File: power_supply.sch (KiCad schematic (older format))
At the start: 20 parts

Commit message: finish scheme & change libs path
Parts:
- gave numbers to parts that had none: 20
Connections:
- net +12V_B renamed FUEL_ADC_POWER
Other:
- note added: "two separate module on 1 PCB\n- module B powered from Vbatt\n- module A powered from IGN\n(Vbatt present always)"

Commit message: specify footpints to resistors and capasitors
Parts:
- C1, C2, C3, C4, C5, C6, C7, C8: footprint (none) -> Capacitors_SMD:C_0805
- U2: footprint TO_SOT_Packages_SMD:TO-263-5_TabPin6 -> zulljon:TO170P1435X457-6N
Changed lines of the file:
@@
 Vbatt
 $Comp
-L GND #PWR05
+L GND #PWR5
 U 1 1 5A05B33F
 P 2400 5550
-F 0 "#PWR05" H 2400 5300 50  0001 C CNN
+F 0 "#PWR5" H 2400 5300 50  0001 C CNN
 F 1 "GND" H 2400 5400 50  0000 C CNN
 F 2 "" H 2400 5550 50  0001 C CNN
@@
 F 0 "C1" H 2475 2250 50  0000 L CNN
 F 1 "100uF" H 2475 2050 50  0000 L CNN
-F 2 "" H 2488 2000 50  0001 C CNN
+F 2 "Capacitors_SMD:C_0805" H 2488 2000 50  0001 C CNN
 F 3 "" H 2450 2150 50  0001 C CNN
 	1    2450 2150
@@
 F 0 "C3" H 5025 2250 50  0000 L CNN
 F 1 "330uF" H 5025 2050 50  0000 L CNN
-F 2 "" H 5038 2000 50  0001 C CNN
+F 2 "Capacitors_SMD:C_0805" H 5038 2000 50  0001 C CNN
 F 3 "" H 5000 2150 50  0001 C CNN
 	1    5000 2150
@@
 	2450 2350 2450 2300
 $Comp
-L GND #PWR06
+L GND #PWR6
 U 1 1 5A05C84D
 P 2550 2400
-F 0 "#PWR06" H 2550 2150 50  0001 C CNN
+F 0 "#PWR6" H 2550 2150 50  0001 C CNN
 F 1 "GND" H 2550 2250 50  0000 C CNN
 F 2 "" H 2550 2400 50  0001 C CNN
@@
 F 0 "C5" H 8325 2200 50  0000 L CNN
 F 1 "100nF" H 8325 2000 50  0000 L CNN
-F 2 "" H 8338 1950 50  0001 C CNN
+F 2 "Capacitors_SMD:C_0805" H 8338 1950 50  0001 C CNN
 F 3 "" H 8300 2100 50  0001 C CNN
 	1    8300 2100
@@
 F 0 "C7" H 9125 2200 50  0000 L CNN
 F 1 "10uF" H 9125 2000 50  0000 L CNN
-F 2 "" H 9138 1950 50  0001 C CNN
+F 2 "Capacitors_SMD:C_0805" H 9138 1950 50  0001 C CNN
 F 3 "" H 9100 2100 50  0001 C CNN
 	1    9100 2100
@@
 	9000 1850 9450 1850
 $Comp
-L GND #PWR07
+L GND #PWR8
 U 1 1 5A05D4B4
 P 8300 2350
-F 0 "#PWR07" H 8300 2100 50  0001 C CNN
+F 0 "#PWR8" H 8300 2100 50  0001 C CNN
 F 1 "GND" H 8300 2200 50  0000 C CNN
 F 2 "" H 8300 2350 50  0001 C CNN
@@
 $EndComp
 $Comp
-L GND #PWR08
+L GND #PWR10
 U 1 1 5A05D4E4
 P 9100 2350
-F 0 "#PWR08" H 9100 2100 50  0001 C CNN
+F 0 "#PWR10" H 9100 2100 50  0001 C CNN
 F 1 "GND" H 9100 2200 50  0000 C CNN
 F 2 "" H 9100 2350 50  0001 C CNN
@@
 F 0 "C6" H 8325 3250 50  0000 L CNN
 F 1 "100nF" H 8325 3050 50  0000 L CNN
-F 2 "" H 8338 3000 50  0001 C CNN
+F 2 "Capacitors_SMD:C_0805" H 8338 3000 50  0001 C CNN
 F 3 "" H 8300 3150 50  0001 C CNN
 	1    8300 3150
@@
 F 0 "C8" H 9125 3250 50  0000 L CNN
 F 1 "10uF" H 9125 3050 50  0000 L CNN
-F 2 "" H 9138 3000 50  0001 C CNN
+F 2 "Capacitors_SMD:C_0805" H 9138 3000 50  0001 C CNN
 F 3 "" H 9100 3150 50  0001 C CNN
 	1    9100 3150
@@
 	9000 2900 9450 2900
 $Comp
-L GND #PWR09
+L GND #PWR9
 U 1 1 5A05D86B
 P 8300 3400
-F 0 "#PWR09" H 8300 3150 50  0001 C CNN
+F 0 "#PWR9" H 8300 3150 50  0001 C CNN
 F 1 "GND" H 8300 3250 50  0000 C CNN
 F 2 "" H 8300 3400 50  0001 C CNN
@@
 $EndComp
 $Comp
-L GND #PWR010
+L GND #PWR11
 U 1 1 5A05D871
 P 9100 3400
-F 0 "#PWR010" H 9100 3150 50  0001 C CNN
+F 0 "#PWR11" H 9100 3150 50  0001 C CNN
 F 1 "GND" H 9100 3250 50  0000 C CNN
 F 2 "" H 9100 3400 50  0001 C CNN
@@
 F 0 "C2" H 2525 3400 50  0000 L CNN
 F 1 "100uF" H 2525 3200 50  0000 L CNN
-F 2 "" H 2538 3150 50  0001 C CNN
+F 2 "Capacitors_SMD:C_0805" H 2538 3150 50  0001 C CNN
 F 3 "" H 2500 3300 50  0001 C CNN
 	1    2500 3300
@@
 F 0 "C4" H 5075 3400 50  0000 L CNN
 F 1 "330uF" H 5075 3200 50  0000 L CNN
-F 2 "" H 5088 3150 50  0001 C CNN
+F 2 "Capacitors_SMD:C_0805" H 5088 3150 50  0001 C CNN
 F 3 "" H 5050 3300 50  0001 C CNN
 	1    5050 3300
@@
 	2500 3500 2500 3450
 $Comp
-L GND #PWR011
+L GND #PWR7
 U 1 1 5A0729CF
 P 2600 3550
-F 0 "#PWR011" H 2600 3300 50  0001 C CNN
+F 0 "#PWR7" H 2600 3300 50  0001 C CNN
 F 1 "GND" H 2600 3400 50  0000 C CNN
 F 2 "" H 2600 3550 50  0001 C CNN
@@
 F 0 "U2" H 3550 3100 50  0000 C CNN
 F 1 "LM2575S-5.0_NOPB" H 3550 2600 50  0000 C CNN
-F 2 "TO_SOT_Packages_SMD:TO-263-5_TabPin6" H 3550 2500 50  0001 C CNN
+F 2 "zulljon:TO170P1435X457-6N" H 3550 2500 50  0001 C CNN
 F 3 "http://www.ti.com/lit/gpn/lm2575" H 3550 2400 50  0001 C CNN
 F 4 "SIMPLE SWITCHER 1.23V to 37V, 1A Low Component Count Step-Down Regulator" H 3550 2300 50  0001 C CNN "Description"

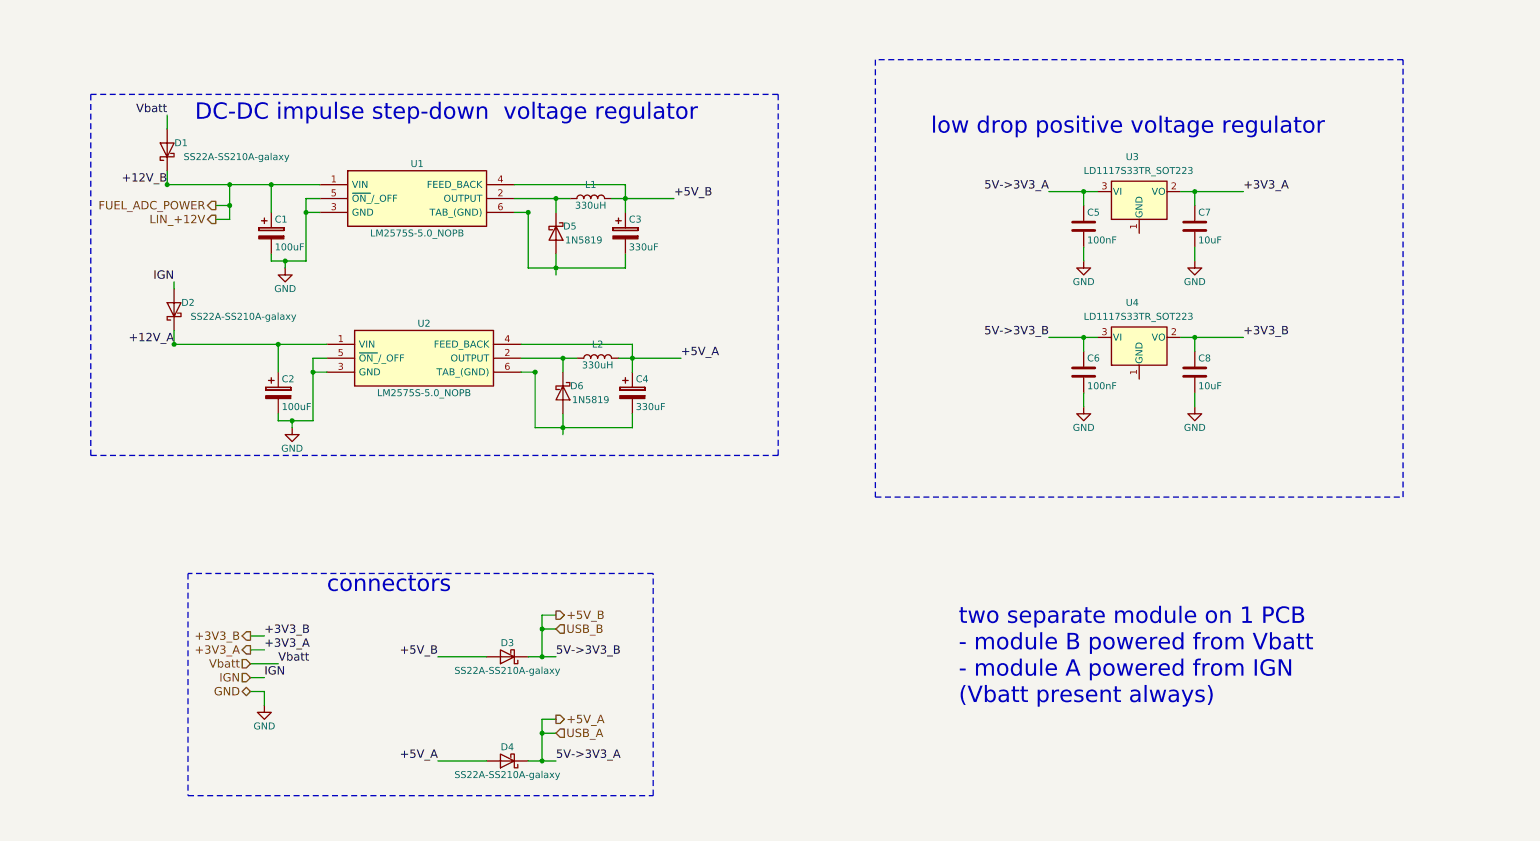
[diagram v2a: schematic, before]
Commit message: add missed footprints, add additional capasitors on 3.3V line, fix banch of ERC errors
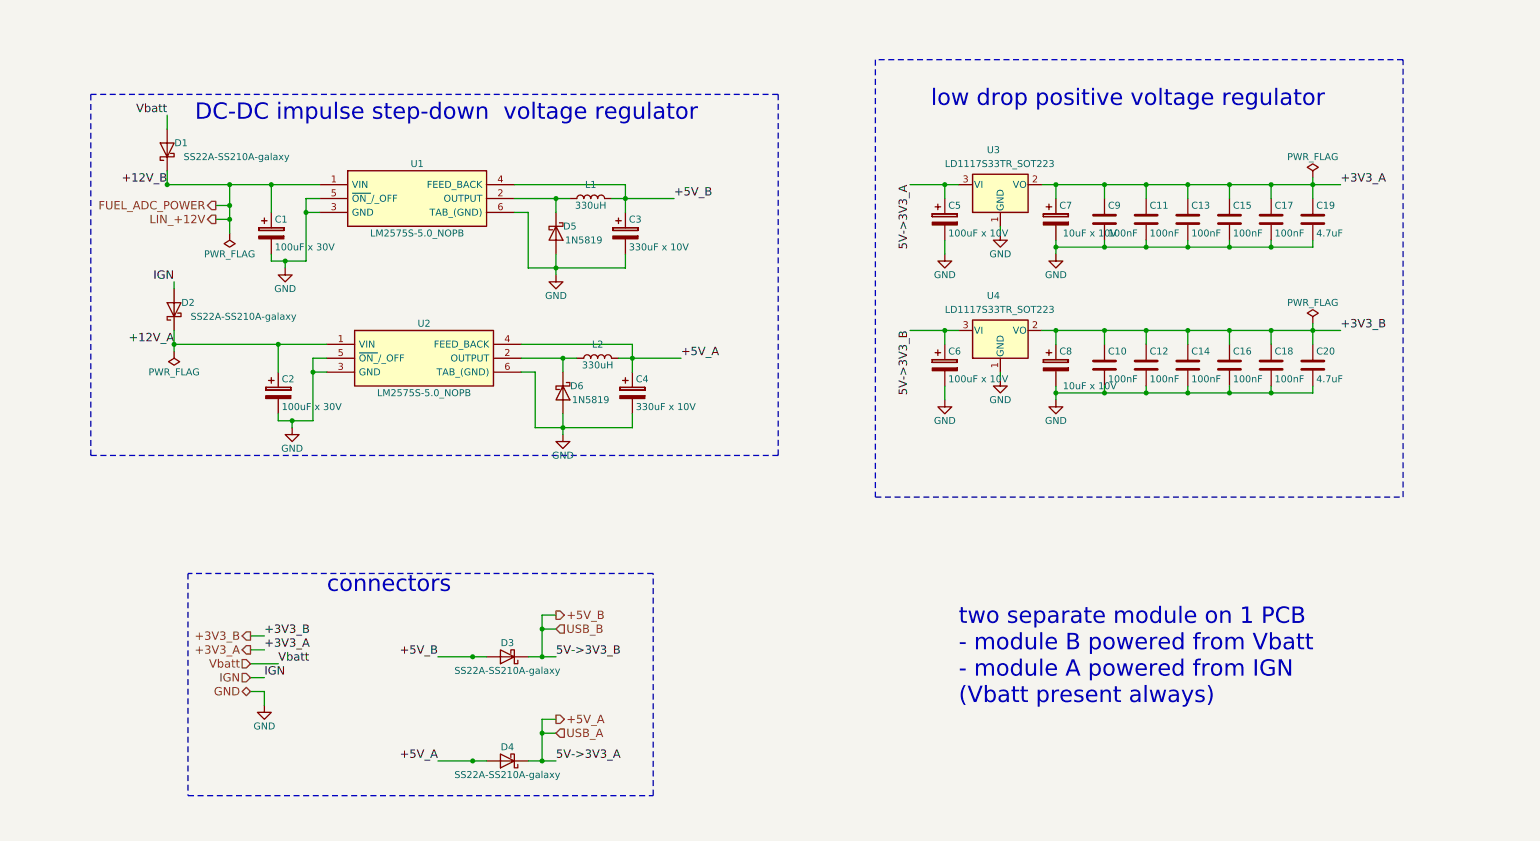
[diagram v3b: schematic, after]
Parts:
- removed C5, C6: 100nF, Capacitors_SMD:C_0805, symbol C
- removed C8: 10uF, Capacitors_SMD:C_0805, symbol C
- added C10, C11, C12, C13, C14, C15, C16, C17, C18, C9: 100nF, Capacitors_SMD:C_0805, symbol C
- added C20: 4.7uF, Capacitors_SMD:C_0805, symbol C
- added C5, C6: 100uF x 10V, Capacitors_Tantalum_SMD:CP_Tantalum_Case-D_EIA-7343-31_Hand, symbol CP
- added C7, C8: 10uF x 10V, Capacitors_Tantalum_SMD:CP_Tantalum_Case-B_EIA-3528-21_Wave, symbol CP
- C1, C2: value 100uF -> 100uF x 30V; footprint Capacitors_SMD:C_0805 -> Capacitors_SMD:CP_Elec_6.3x7.7; imrad (none) -> ECAPSMD 100/25V 0608
- C19: renamed from C7; value 10uF -> 4.7uF
- C3, C4: value 330uF -> 330uF x 10V; footprint Capacitors_SMD:C_0805 -> Capacitors_SMD:CP_Elec_8x10
- L1, L2: footprint (none) -> Inductors_SMD:L_12x12mm_h8mm
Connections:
- net +3V3_A: now also C11.1, C13.1, C15.1, C17.1, C7.1, C9.1
- net +3V3_B: now also C10.1, C12.1, C14.1, C16.1, C18.1, C20.1, C8.1
- net +5V_A: now also C5.1
- net +5V_B: now also C6.1
- net GND: now also C3.2, C4.2, D5.2 (A), D6.2 (A), U1.6 (TAB_(GND)), U2.6 (TAB_(GND)), U3.1 (GND), U4.1 (GND), C10.2, C11.2, C12.2, C13.2, C14.2, C15.2, C16.2, C17.2, C18.2, C20.2, C5.2, C6.2, C7.2, C8.2, C9.2
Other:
- moved on the sheet: C19, U3, U4

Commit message: delete LIN, fix ERC errors
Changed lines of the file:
@@
 Vbatt
 $Comp
-L GND #PWR05
+L GND #PWR06
 U 1 1 5A05B33F
 P 2400 5550
-F 0 "#PWR05" H 2400 5300 50  0001 C CNN
+F 0 "#PWR06" H 2400 5300 50  0001 C CNN
 F 1 "GND" H 2400 5400 50  0000 C CNN
 F 2 "" H 2400 5550 50  0001 C CNN
@@
 $EndComp
 $Comp
-L GND #PWR06
+L GND #PWR07
 U 1 1 5A05C84D
 P 2550 2400
-F 0 "#PWR06" H 2550 2150 50  0001 C CNN
+F 0 "#PWR07" H 2550 2150 50  0001 C CNN
 F 1 "GND" H 2550 2250 50  0000 C CNN
 F 2 "" H 2550 2400 50  0001 C CNN
@@
 $EndComp
 $Comp
-L GND #PWR07
+L GND #PWR08
 U 1 1 5A05D4B4
 P 7300 2300
-F 0 "#PWR07" H 7300 2050 50  0001 C CNN
+F 0 "#PWR08" H 7300 2050 50  0001 C CNN
 F 1 "GND" H 7300 2150 50  0000 C CNN
 F 2 "" H 7300 2300 50  0001 C CNN
@@
 $EndComp
 $Comp
-L GND #PWR08
+L GND #PWR09
 U 1 1 5A05D4E4
 P 8100 2300
-F 0 "#PWR08" H 8100 2050 50  0001 C CNN
+F 0 "#PWR09" H 8100 2050 50  0001 C CNN
 F 1 "GND" H 8100 2150 50  0000 C CNN
 F 2 "" H 8100 2300 50  0001 C CNN
@@
 $EndComp
 $Comp
-L GND #PWR09
+L GND #PWR010
 U 1 1 5A05D86B
 P 7300 3350
-F 0 "#PWR09" H 7300 3100 50  0001 C CNN
+F 0 "#PWR010" H 7300 3100 50  0001 C CNN
 F 1 "GND" H 7300 3200 50  0000 C CNN
 F 2 "" H 7300 3350 50  0001 C CNN
@@
 $EndComp
 $Comp
-L GND #PWR010
+L GND #PWR011
 U 1 1 5A0729CF
 P 2600 3550
-F 0 "#PWR010" H 2600 3300 50  0001 C CNN
+F 0 "#PWR011" H 2600 3300 50  0001 C CNN
 F 1 "GND" H 2600 3400 50  0000 C CNN
 F 2 "" H 2600 3550 50  0001 C CNN
@@
 Text HLabel 2050 1950 0    60   Output ~ 0
 FUEL_ADC_POWER
-Text HLabel 2050 2050 0    60   Output ~ 0
-LIN_+12V
 Text Notes 7400 5550 0    118  ~ 0
 two separate module on 1 PCB\n- module B powered from Vbatt\n- module A powered from IGN\n(Vbatt present always)
 $Comp
-L GND #PWR011
+L GND #PWR012
 U 1 1 5A0D545B
 P 7700 2150
-F 0 "#PWR011" H 7700 1900 50  0001 C CNN
+F 0 "#PWR012" H 7700 1900 50  0001 C CNN
 F 1 "GND" H 7700 2000 50  0000 C CNN
 F 2 "" H 7700 2150 50  0001 C CNN
@@
 $EndComp
 $Comp
-L GND #PWR012
+L GND #PWR013
 U 1 1 5A0D5601
 P 7700 3200
-F 0 "#PWR012" H 7700 2950 50  0001 C CNN
+F 0 "#PWR013" H 7700 2950 50  0001 C CNN
 F 1 "GND" H 7700 3050 50  0000 C CNN
 F 2 "" H 7700 3200 50  0001 C CNN
@@
 $EndComp
 $Comp
-L GND #PWR013
+L GND #PWR014
 U 1 1 5A0D7B4C
 P 8100 3350
-F 0 "#PWR013" H 8100 3100 50  0001 C CNN
+F 0 "#PWR014" H 8100 3100 50  0001 C CNN
 F 1 "GND" H 8100 3200 50  0000 C CNN
 F 2 "" H 8100 3350 50  0001 C CNN
@@
 $EndComp
 $Comp
-L GND #PWR014
+L GND #PWR015
 U 1 1 5A0D9A6D
 P 4500 2450
-F 0 "#PWR014" H 4500 2200 50  0001 C CNN
+F 0 "#PWR015" H 4500 2200 50  0001 C CNN
 F 1 "GND" H 4500 2300 50  0000 C CNN
 F 2 "" H 4500 2450 50  0001 C CNN
@@
 $EndComp
 $Comp
-L GND #PWR015
+L GND #PWR016
 U 1 1 5A0D9AD8
 P 4550 3600
-F 0 "#PWR015" H 4550 3350 50  0001 C CNN
+F 0 "#PWR016" H 4550 3350 50  0001 C CNN
 F 1 "GND" H 4550 3450 50  0000 C CNN
 F 2 "" H 4550 3600 50  0001 C CNN
@@
 	2150 1800 2150 2150
 Connection ~ 2150 1800
-Wire Wire Line
-	2150 2050 2050 2050
 Connection ~ 2150 1950
 Wire Wire Line
@@
 Connection ~ 9950 2850
 $Comp
-L PWR_FLAG #FLG016
+L PWR_FLAG #FLG017
 U 1 1 5A0DF92C
 P 1750 3000
-F 0 "#FLG016" H 1750 3075 50  0001 C CNN
+F 0 "#FLG017" H 1750 3075 50  0001 C CNN
 F 1 "PWR_FLAG" H 1750 3150 50  0000 C CNN
 F 2 "" H 1750 3000 50  0001 C CNN
@@
 $EndComp
 $Comp
-L PWR_FLAG #FLG017
+L PWR_FLAG #FLG018
 U 1 1 5A0DFAF7
 P 2150 2150
-F 0 "#FLG017" H 2150 2225 50  0001 C CNN
+F 0 "#FLG018" H 2150 2225 50  0001 C CNN
 F 1 "PWR_FLAG" H 2150 2300 50  0000 C CNN
 F 2 "" H 2150 2150 50  0001 C CNN
@@
 Connection ~ 2150 2050
 $Comp
-L PWR_FLAG #FLG018
+L PWR_FLAG #FLG019
 U 1 1 5A0DFF23
 P 9950 2800
-F 0 "#FLG018" H 9950 2875 50  0001 C CNN
+F 0 "#FLG019" H 9950 2875 50  0001 C CNN
 F 1 "PWR_FLAG" H 9950 2950 50  0000 C CNN
 F 2 "" H 9950 2800 50  0001 C CNN
@@
 $EndComp
 $Comp
-L PWR_FLAG #FLG019
+L PWR_FLAG #FLG020
 U 1 1 5A0E00D0
 P 9950 1750
-F 0 "#FLG019" H 9950 1825 50  0001 C CNN
+F 0 "#FLG020" H 9950 1825 50  0001 C CNN
 F 1 "PWR_FLAG" H 9950 1900 50  0000 C CNN
 F 2 "" H 9950 1750 50  0001 C CNN

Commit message: fix D3 D4 diods connections
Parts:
- U2: footprint zulljon:TO170P1435X457-6N -> TO_SOT_Packages_SMD:TO-263-5_TabPin6
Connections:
- net +5V_A: no longer C4.1, D4.2 (A), L2.2, U2.4 (FEED_BACK)
- net +5V_B: no longer C3.1, D3.2 (A), L1.2, U1.4 (FEED_BACK)
- new net +5V_A_module: C4.1, D4.2 (A), L2.2, U2.4 (FEED_BACK)
- new net +5V_B_module: C3.1, D3.2 (A), L1.2, U1.4 (FEED_BACK)
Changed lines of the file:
@@
 $EndComp
 Text Label 3650 5200 2    60   ~ 0
-+5V_B
++5V_B_module
 Text Label 1700 1300 2    60   ~ 0
 Vbatt
@@
 $EndComp
 Text Label 3650 5950 2    60   ~ 0
-+5V_A
++5V_A_module
 Text Notes 2850 4750 0    118  ~ 0
 connectors
@@
 F 0 "U2" H 3550 3100 50  0000 C CNN
 F 1 "LM2575S-5.0_NOPB" H 3550 2600 50  0000 C CNN
-F 2 "zulljon:TO170P1435X457-6N" H 3550 2500 50  0001 C CNN
+F 2 "TO_SOT_Packages_SMD:TO-263-5_TabPin6" H 3550 2500 50  0001 C CNN
 F 3 "http://www.ti.com/lit/gpn/lm2575" H 3550 2400 50  0001 C CNN
 F 4 "SIMPLE SWITCHER 1.23V to 37V, 1A Low Component Count Step-Down Regulator" H 3550 2300 50  0001 C CNN "Description"
@@
 $EndComp
 Text Label 5350 1900 0    60   ~ 0
-+5V_B
++5V_B_module
 Text Label 5400 3050 0    60   ~ 0
-+5V_A
++5V_A_module
 Text HLabel 2050 1950 0    60   Output ~ 0
 FUEL_ADC_POWER

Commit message: add commentary to scheme
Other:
- note added: "C10 C12 C14 C16 C18 C20\nmust be near the power pins of MCU"
- note added: "C7 C11 C13 C15 C17 C19\nmust be near the power pins of MCU"
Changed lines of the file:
@@
 Connection ~ 8750 3300
 Connection ~ 8450 3300
+Text Notes 8450 2500 0    60   ~ 0
+C7 C11 C13 C15 C17 C19\nmust be near the power pins of MCU
+Text Notes 8450 3550 0    60   ~ 0
+C10 C12 C14 C16 C18 C20\nmust be near the power pins of MCU
 $EndSCHEMATC
